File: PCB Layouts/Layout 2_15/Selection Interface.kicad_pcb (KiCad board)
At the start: 4 copper layers, 110 x 90 mm, 132 parts, among them P1 CONN_01X02, P11 CONN_01X02, P12 CONN_01X02, P13 CONN_01X10, P14 CONN_01X02, P15 CONN_01X02, P16 CONN_01X02, P18 CONN_02X05, P19 CONN_02X05, P2 CONN_01X02, P21 CONN_02X05, P3 CONN_01X02, P4 CONN_01X02, P5 CONN_01X02, P6 CONN_02X10, P7 CONN_01X02, P8 CONN_02X04, P9 CONN_01X02

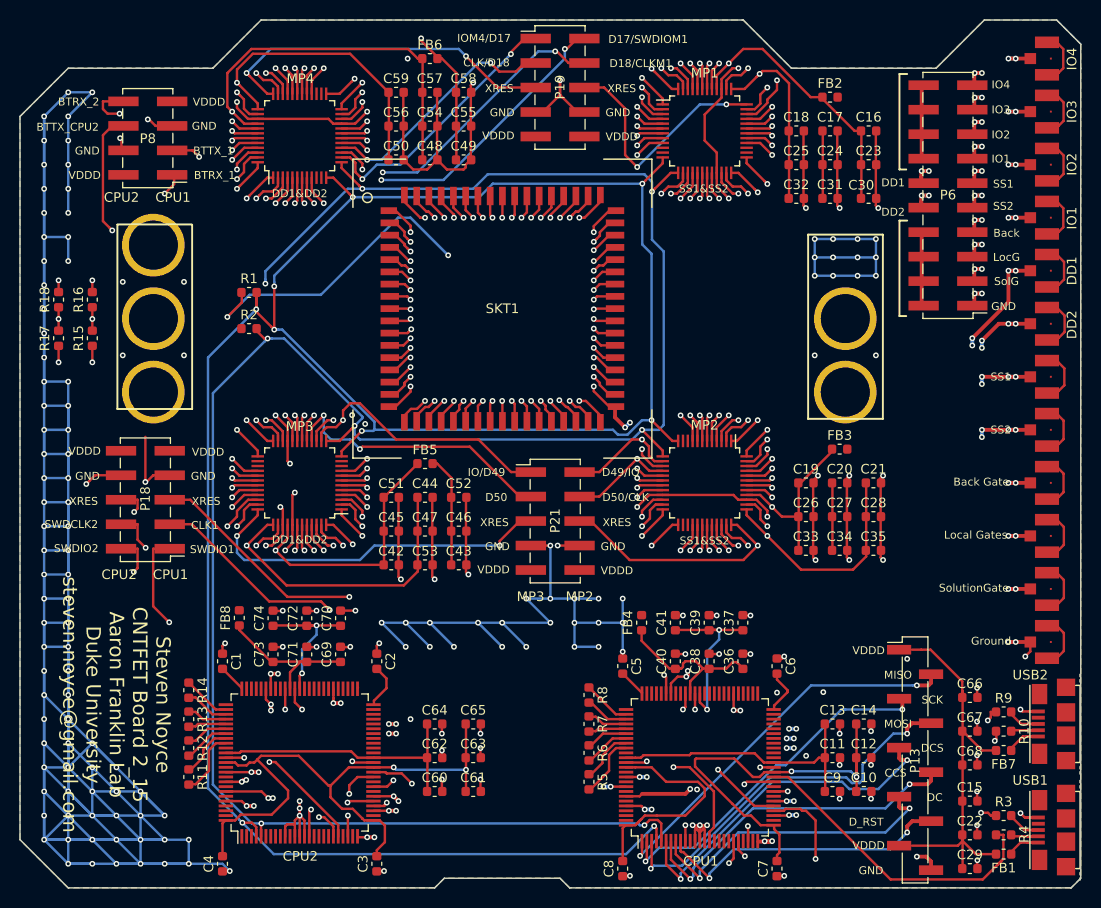
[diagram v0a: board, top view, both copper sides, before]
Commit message: Renamed the multiplexers in Layout 2_15
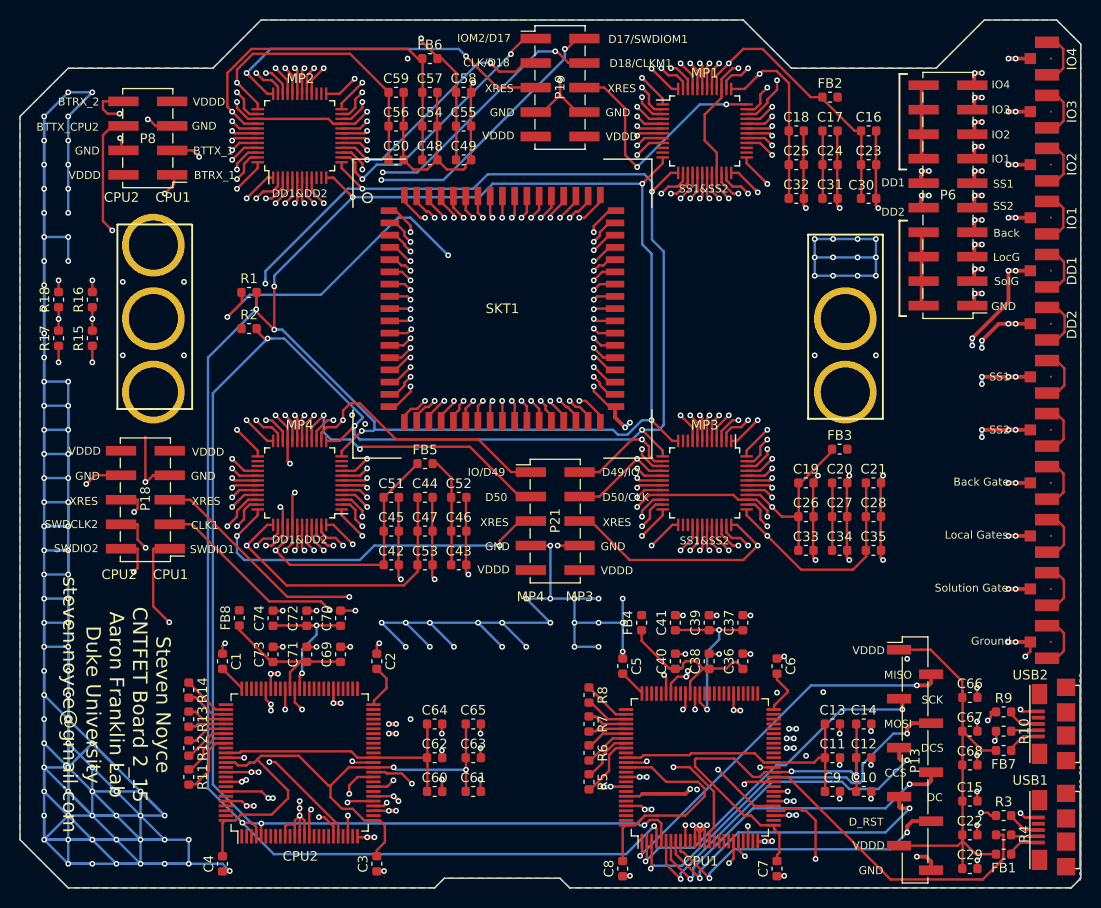
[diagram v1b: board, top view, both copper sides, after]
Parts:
- moved MP2 55.3 mm to (179.0, 82.0), turned to 90 degrees
- moved MP3 42.0 mm to (221.0, 118.0), turned to 270 degrees
- moved MP4 36.0 mm to (179.0, 118.0), turned to 180 degrees
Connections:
- MP2 pad 1: D40 -> D8
- MP2 pad 14: D49 -> D17P
- MP2 pad 16: D50 -> D18P
- MP2 pad 17: D51 -> D19
- MP2 pad 18: D52 -> D20
- MP2 pad 19: D53 -> D21
- MP2 pad 2: D41 -> D9
- MP2 pad 20: D54 -> D22
- MP2 pad 22: D55 -> D23
- MP2 pad 23: D56 -> D24
- MP2 pad 24: D57 -> D25
- MP2 pad 25: D58 -> D26
- MP2 pad 28: D59 -> D27
- MP2 pad 29: D60 -> D28
- MP2 pad 3: D42 -> D10
- MP2 pad 30: D61 -> D29
- MP2 pad 31: D62 -> D30
- MP2 pad 32: D63 -> D31
- MP2 pad 33: D64 -> D32
- MP2 pad 34: SS1 -> DD1
- MP2 pad 35: SS2 -> DD2
- MP2 pad 36: XRES4 -> XRES2
- MP2 pad 37: Net-(C21-Pad1) -> Net-(C50-Pad1)
- MP2 pad 4: D43 -> D11
- MP2 pad 40: Net-(C19-Pad1) -> Net-(C48-Pad1)
- MP2 pad 42: D33 -> D1
- MP2 pad 43: D34 -> D2
- MP2 pad 44: D35 -> D3
- MP2 pad 45: D36 -> D4
- MP2 pad 46: D37 -> D5
- MP2 pad 47: D38 -> D6
- MP2 pad 48: D39 -> D7
- MP2 pad 5: D44 -> D12
- MP2 pad 6: D45 -> D13
- MP2 pad 7: D46 -> D14
- MP2 pad 8: D47 -> D15
- MP2 pad 9: D48 -> D16
- MP3 pad 14: D49P -> D49
- MP3 pad 16: D50P -> D50
- MP3 pad 34: DD1 -> SS1
- MP3 pad 35: DD2 -> SS2
- MP3 pad 36: XRES3 -> XRES4
- MP3 pad 37: Net-(C44-Pad1) -> Net-(C21-Pad1)
- MP3 pad 40: Net-(C42-Pad1) -> Net-(C19-Pad1)
- MP4 pad 1: D8 -> D40
- MP4 pad 14: D17P -> D49P
- MP4 pad 16: D18P -> D50P
- MP4 pad 17: D19 -> D51
- MP4 pad 18: D20 -> D52
- MP4 pad 19: D21 -> D53
- MP4 pad 2: D9 -> D41
- MP4 pad 20: D22 -> D54
- MP4 pad 22: D23 -> D55
- MP4 pad 23: D24 -> D56
- MP4 pad 24: D25 -> D57
- MP4 pad 25: D26 -> D58
- MP4 pad 28: D27 -> D59
- MP4 pad 29: D28 -> D60
- MP4 pad 3: D10 -> D42
- MP4 pad 30: D29 -> D61
- MP4 pad 31: D30 -> D62
- MP4 pad 32: D31 -> D63
- MP4 pad 33: D32 -> D64
- MP4 pad 36: XRES2 -> XRES3
- MP4 pad 37: Net-(C50-Pad1) -> Net-(C44-Pad1)
- MP4 pad 4: D11 -> D43
- MP4 pad 40: Net-(C48-Pad1) -> Net-(C42-Pad1)
- MP4 pad 42: D1 -> D33
- MP4 pad 43: D2 -> D34
- MP4 pad 44: D3 -> D35
- MP4 pad 45: D4 -> D36
- MP4 pad 46: D5 -> D37
- MP4 pad 47: D6 -> D38
- MP4 pad 48: D7 -> D39
- MP4 pad 5: D12 -> D44
- MP4 pad 6: D13 -> D45
- MP4 pad 7: D14 -> D46
- MP4 pad 8: D15 -> D47
- MP4 pad 9: D16 -> D48
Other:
- board text added: "IOM2/D17"
- board text added: "MP4"
- board text added: "Solution Gate"
- board text removed: "IOM4/D17"
- board text removed: "MP2"
- board text removed: "SolutionGate"

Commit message: Added a new compoent to try to reduce the area taken up by programming headers. Began making some wiring changes to facilitate this
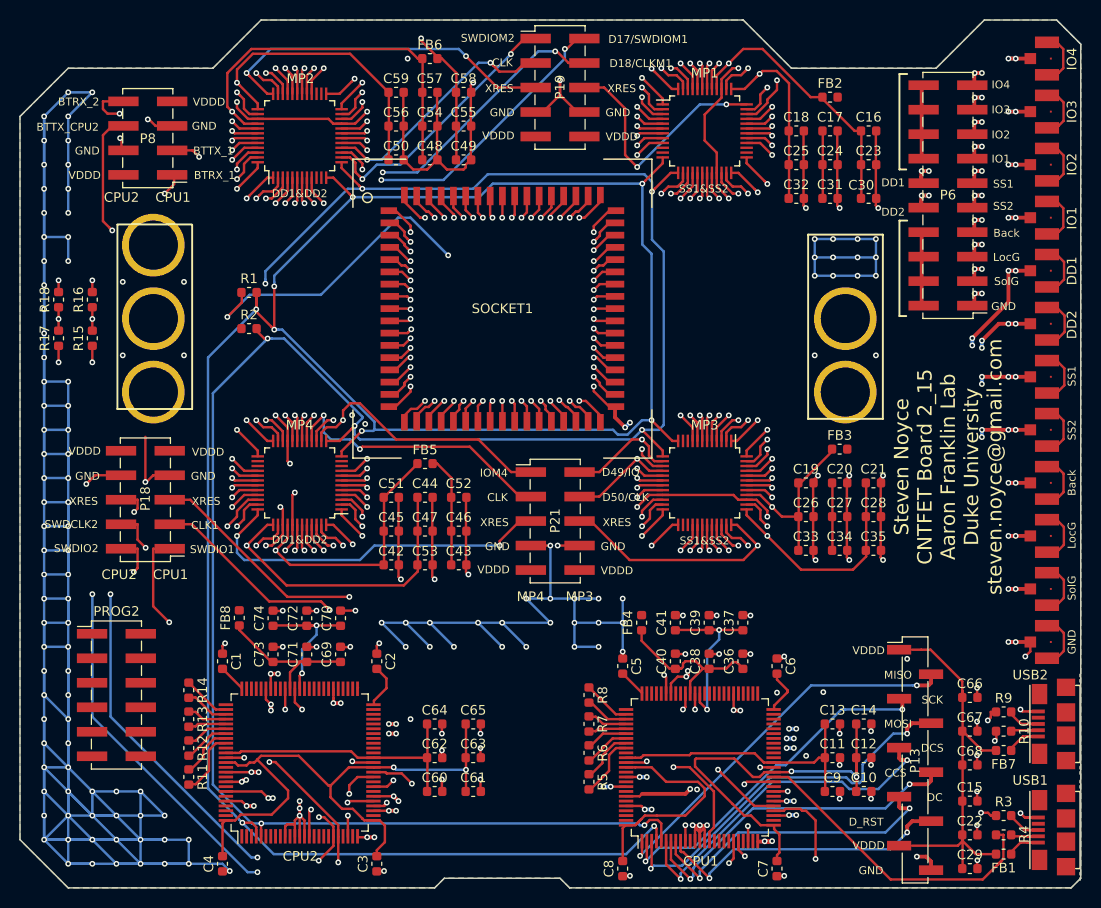
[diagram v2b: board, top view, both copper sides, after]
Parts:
- removed SKT1: 68_PLCC_Socket_(8468-21B1-RK-TP), Custom_Footprint_Library:68_PLCC_Socket_(8468-21B1-RK-TP)
- added PROG2: Conn_02x06_Odd_Even, Connector_PinHeader_2.54mm:PinHeader_2x06_P2.54mm_Vertical_SMD, F.Cu at (160.0, 140.0)
- added SOCKET1: 68_PLCC_Socket_(8468-21B1-RK-TP), Custom_Footprint_Library:68_PLCC_Socket_(8468-21B1-RK-TP), F.Cu at (200.0, 99.9)
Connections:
- net D17P renamed SWDIO2
- net D18P renamed SWDCLK2
- net D49P renamed SWDIO4
- net D50P renamed SWDCLK4
- MP3 pad 36: XRES4 -> XRES3
- MP4 pad 36: XRES3 -> XRES4
- P21 pad 5: XRES3 -> XRES4
- P21 pad 6: XRES4 -> XRES3
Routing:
- net GND: track 828.0 -> 790.2 mm, vias 219 -> 216
- net BT2_TX: track 95.3 -> 110.6 mm, vias 2 -> 4
- net XRES4: track 24.2 -> 37.9 mm, vias 1 -> 2
- net XRES3: track 37.9 -> 24.2 mm, vias 2 -> 1
- net SWDIO6: track 45.5 -> 48.7 mm, vias 2 -> 3
- net SWDCLK6: track 43.3 -> 46.0 mm, vias 2 -> 3
- net BT1_RX: track 129.8 -> 131.7 mm, vias 2 -> 4
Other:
- board text added: "CLK"
- board text added: "IOM4"
- board text added: "SWDIOM2"
- board text removed: "Back Gate"
- board text removed: "CLK/D18"
- board text removed: "D50"
- board text removed: "Ground"
- board text removed: "IO/D49"
- board text removed: "IOM2/D17"
- board text removed: "Local Gates"
- board text removed: "Solution Gate"

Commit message: Added more routing to layout 2_15
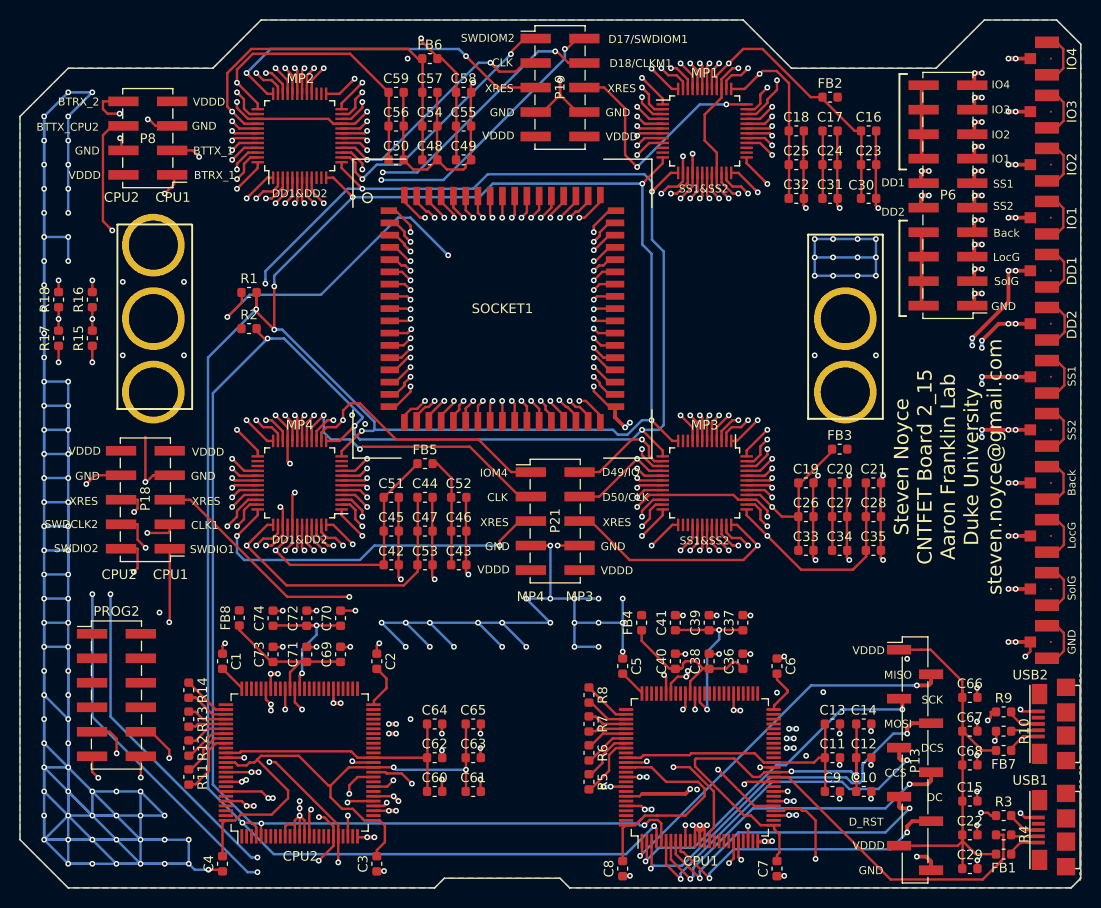
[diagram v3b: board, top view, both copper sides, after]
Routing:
- net SWDCLK6: track 46.0 -> 77.4 mm, vias 3 -> 4
- net SWDCLK5: track 75.5 -> 106.0 mm, vias 2 -> 4
- net SWDIO6: track 48.7 -> 73.1 mm, vias 3 -> 4
- net SWDIO5: track 89.3 -> 91.3 mm, vias 2 -> 3
- net D18: track 67.9 -> 69.9 mm, vias 4 -> 5
- net D17: track 67.5 -> 69.2 mm, vias 4 -> 5
- net GND: track 790.2 -> 788.8 mm
- net Net-(CPU2-Pad36): track 79.6 -> 78.4 mm

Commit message: Updated a lot of routing on layout 2_15 to organize digital signals into certain bus areas far away from analog signals. This is also to make room for additional routing coming soon
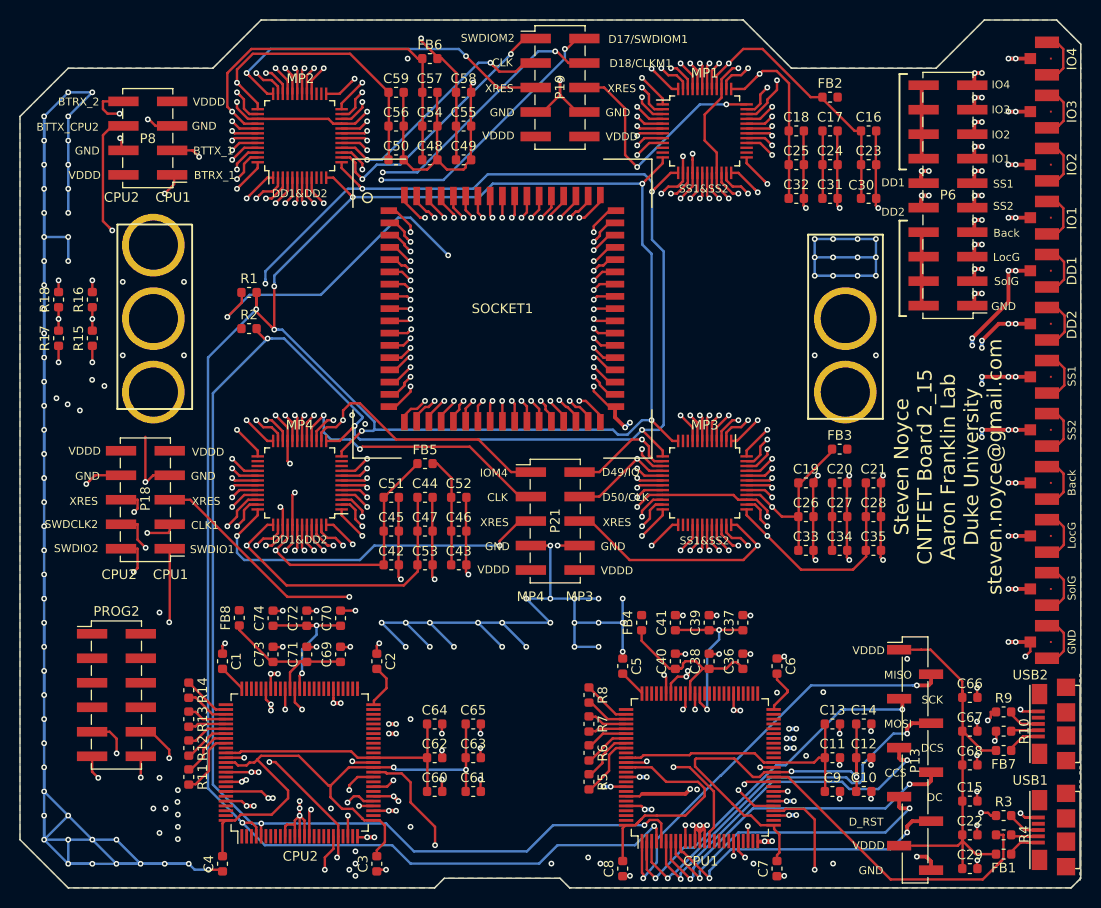
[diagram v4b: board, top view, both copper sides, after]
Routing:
- net GND: track 788.8 -> 591.2 mm, vias 216 -> 188
- net BT1_TX: track 116.5 -> 164.1 mm, vias 2 -> 8
- net SWDIO6: track 73.1 -> 57.4 mm
- net BT2_RX: track 66.2 -> 77.3 mm, vias 2 -> 4
- net BT1_RX: track 131.7 -> 139.3 mm, vias 4 -> 6
- net SWDCLK5: track 106.0 -> 112.1 mm, vias 4 -> 8
- net Net-(CPU2-Pad35): track 81.4 -> 87.2 mm, vias 2 -> 3
- net BT2_TX: track 110.6 -> 105.3 mm, vias 4 -> 5
- net DisplayMISO: track 40.1 -> 44.5 mm
- net Net-(CPU2-Pad36): track 78.4 -> 82.4 mm, vias 2 -> 4
- net DisplaySCK: track 36.5 -> 40.3 mm
- net I2C0_SDA: track 242.2 -> 244.5 mm
- net Net-(P8-Pad1): track 22.4 -> 24.6 mm
- net SWDIO5: track 91.3 -> 93.1 mm, vias 3 -> 5
- net SWDCLK6: track 77.4 -> 76.2 mm
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
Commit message: Did more signal routing and organizing in Layout 2_15
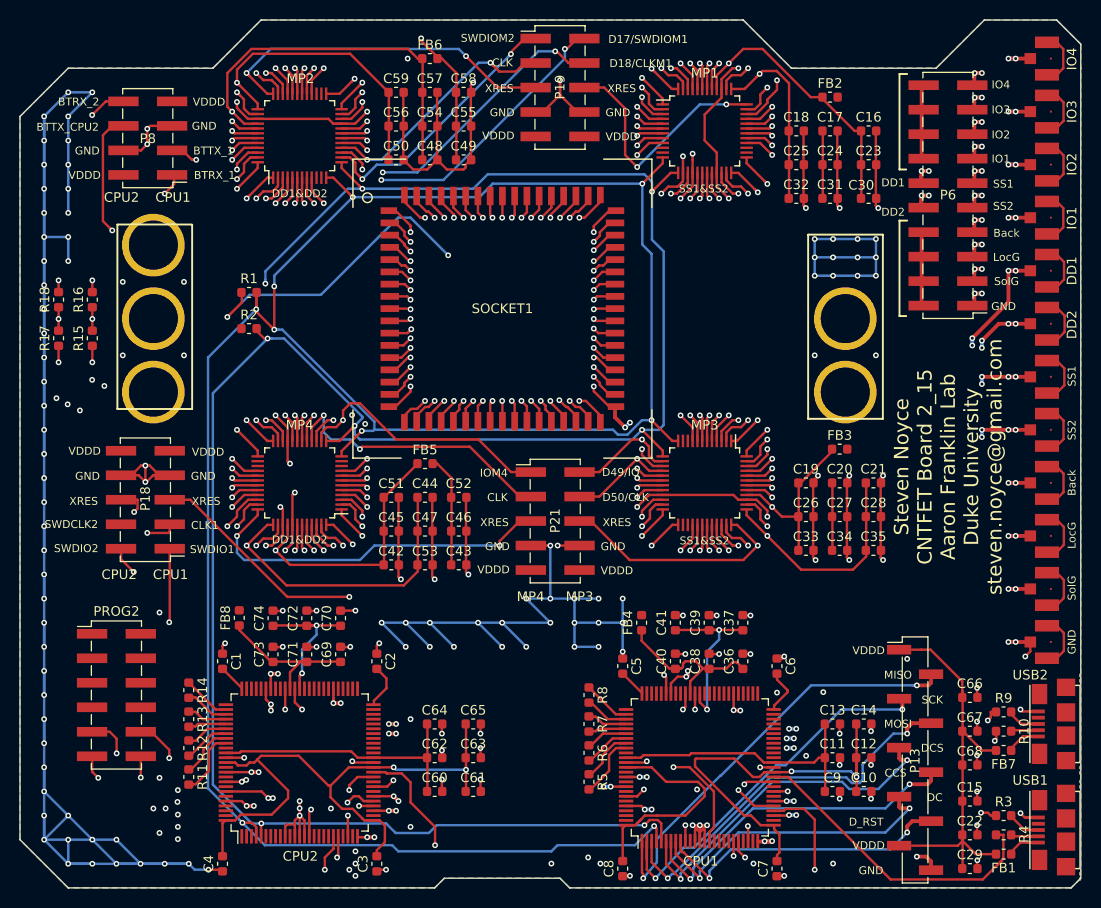
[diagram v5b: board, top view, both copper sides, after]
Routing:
- net SWDCLK6: track 76.2 -> 32.9 mm, vias 4 -> 2
- net GND: track 591.2 -> 595.9 mm
- net Net-(P8-Pad8): track 31.0 -> 28.9 mm
- net I2C0_SDA: track 244.5 -> 242.9 mm
- net SWDIO6: track 57.4 -> 55.9 mm
- net I2C0_SCL: track 246.7 -> 245.6 mm

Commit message: Did more routing on layout 2_15
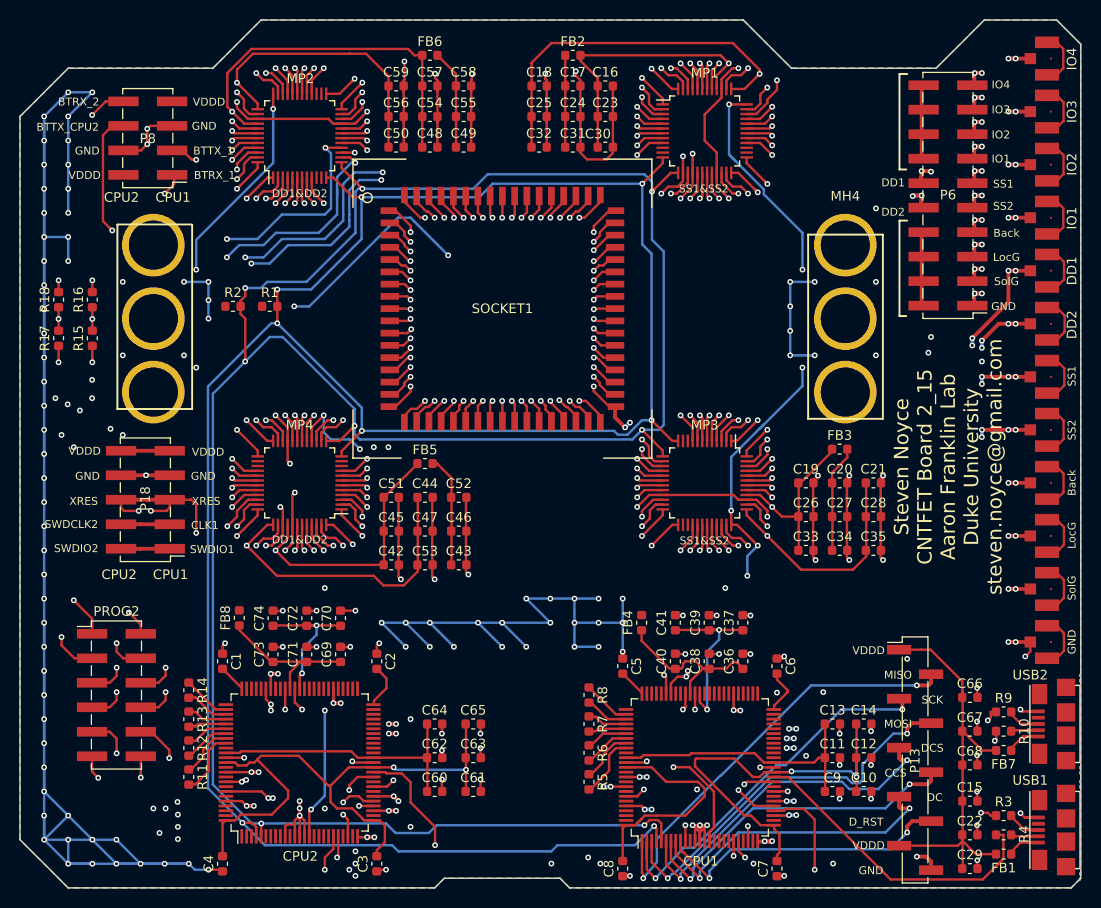
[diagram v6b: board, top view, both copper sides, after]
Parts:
- removed P19, P21: CONN_02X05, Connector_PinHeader_2.54mm:PinHeader_2x05_P2.54mm_Vertical_SMD
- added MH4: MountingHole, Custom_Footprint_Library:MountingHole_5.1mm, F.Cu at (235.6, 93.3)
- moved C30 27.8 mm to (210.7, 83.2)
- moved C23 27.8 mm to (210.7, 80.0)
- moved C16 27.7 mm to (210.7, 76.8)
- moved C31 27.2 mm to (207.3, 83.2)
- moved C32 27.2 mm to (203.8, 83.2)
- moved C24 27.1 mm to (207.3, 80.0)
- moved C25 27.1 mm to (203.8, 80.0)
- moved C17 27.1 mm to (207.3, 76.8)
- moved C18 27.1 mm to (203.8, 76.8)
- moved FB2 27.0 mm to (207.3, 73.7), turned to 180 degrees
- moved R2 2.84 mm to (172.1, 99.7)
- moved R1 2.59 mm to (175.9, 99.7)
- moved C48 1.31 mm to (192.5, 83.2)
- moved C49 1.31 mm to (196.0, 83.2)
- moved C50 1.31 mm to (189.0, 83.2)
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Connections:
- CPU1 pad 15: XRES5 -> XRES
- CPU2 pad 15: XRES6 -> XRES
- MP1 pad 36: XRES1 -> XRES
- MP2 pad 36: XRES2 -> XRES
- MP3 pad 36: XRES3 -> XRES
- MP4 pad 36: XRES4 -> XRES
- P18 pad 1: SWDIO5 -> SWDIO
- P18 pad 2: SWDIO6 -> SWDIO
- P18 pad 3: SWDCLK5 -> SWDCLK
- P18 pad 4: SWDCLK6 -> SWDCLK
- P18 pad 5: XRES5 -> XRES
- P18 pad 6: XRES6 -> XRES
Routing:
- net XRES: track 0.00 -> 250.6 mm, vias 0 -> 18
- net XRES5: track 74.1 -> 0.00 mm, vias 2 -> 0
- net SWDCLK2: track 25.4 -> 87.6 mm, vias 2 -> 4
- net D18: track 69.9 -> 125.9 mm, vias 5 -> 7
- net XRES6: track 50.2 -> 0.00 mm, vias 2 -> 0
- net SWDIO2: track 27.6 -> 75.5 mm, vias 2 -> 4
- net D17: track 69.2 -> 111.5 mm, vias 5 -> 7
- net GND: track 595.9 -> 557.1 mm, vias 188 -> 183
- net XRES4: track 37.9 -> 0.00 mm, vias 2 -> 0
- net XRES2: track 36.1 -> 0.00 mm, vias 2 -> 0
- net SWDCLK5: track 112.1 -> 79.6 mm, vias 8 -> 5
- net XRES1: track 25.6 -> 0.00 mm, vias 2 -> 0
- net SWDIO6: track 55.9 -> 31.3 mm, vias 4 -> 3
- net XRES3: track 24.2 -> 0.00 mm, vias 1 -> 0
- net SWDIO5: track 93.1 -> 69.9 mm, vias 5 -> 3
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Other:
- board text removed: "CLK"
- board text removed: "D17/SWDIOM1"
- board text removed: "D18/CLKM1"
- board text removed: "D49/IO"
- board text removed: "D50/CLK"
- board text removed: "IOM4"
- board text removed: "MP3"
- board text removed: "MP4"
- board text removed: "SWDIOM2"
